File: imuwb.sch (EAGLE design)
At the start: 13 parts

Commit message: new version
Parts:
- added C4: 100nf, ipc-7351-capacitor:CAPACITOR_0402
- added U$1: MIC53533.3V, bell-card:MIC53533.3V
- added U$2: BATPADS, custom:BATPADS
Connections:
- net CSE renamed CS_ENV
- removed net CS: DWM.CS, MCP2210.GP6
- removed net CSB: BMF.PA00, MCP2210.GP2
- removed net IRQ: BMF.PA22, DWM.GPIO8/IRQ
- removed net RSTN: DWM.RSTN
- removed net RST_MCP: BMF.PA20, MCP2210.RST, R1.1
- removed net SUSP: BMF.PA01, MCP2210.GP1
- new net CS_ACC: BMF.PA18/CSB_ACC, MCP2210.GP0
- new net CS_DWM: DWM.CS, MCP2210.GP7
- new net CS_GYR: BMF.PA27/CSB_GYRO, MCP2210.GP1
- new net IRQ_DW: BMF.PA22, DWM.GPIO8/IRQ, MCP2210.GP6
- new net N$4: C4.2, U$1.BYP
- new net N$5: MCP2210.RST, R1.1
- new net VBAT: AAT3681.BAT, C3.1, U$1.EN, U$1.VIN, U$2.-
- net +3V3: now also MCP2210.VUSB, U$1.VOUT; no longer AAT3681.BAT, AAT3681.EN, BMF.PB02, C3.2
- net GND: now also C3.2, C4.1, U$1.GND, U$1.GND1, U$2.+; no longer C3.1
- net RESET: now also DWM.RSTN, MCP2210.GP2
- net VBUS: now also AAT3681.EN; no longer MCP2210.VUSB
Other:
- note added: "ERRATA:"
- note added: "battery connector"
- note added: "voltage regulator"
- note removed: "ERRATA: * GP2 is USB SUSPEND, exchange GP1/GP2 * GP6 is IRQIN, wire to IRQ * wire RST pins for initialization? * move pins below mcp2210"
- note removed: "bat charge estimation"
- note removed: "necc to regulate voltage level below 4.2v all time (i.e. when USB only, when BAT only, when USB+BAT)"
- moved on the sheet: C3

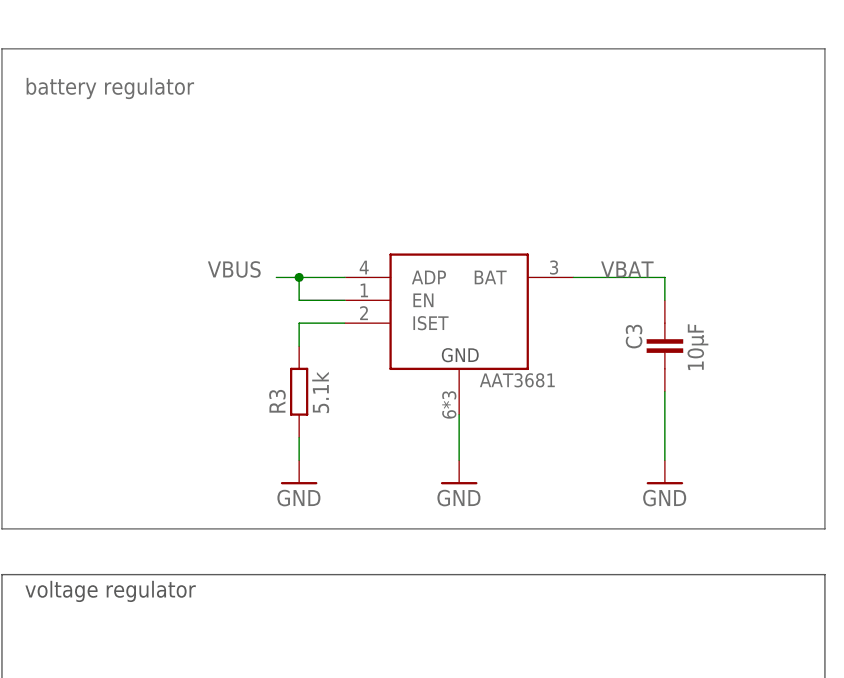
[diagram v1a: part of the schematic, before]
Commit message: updates to the BOM
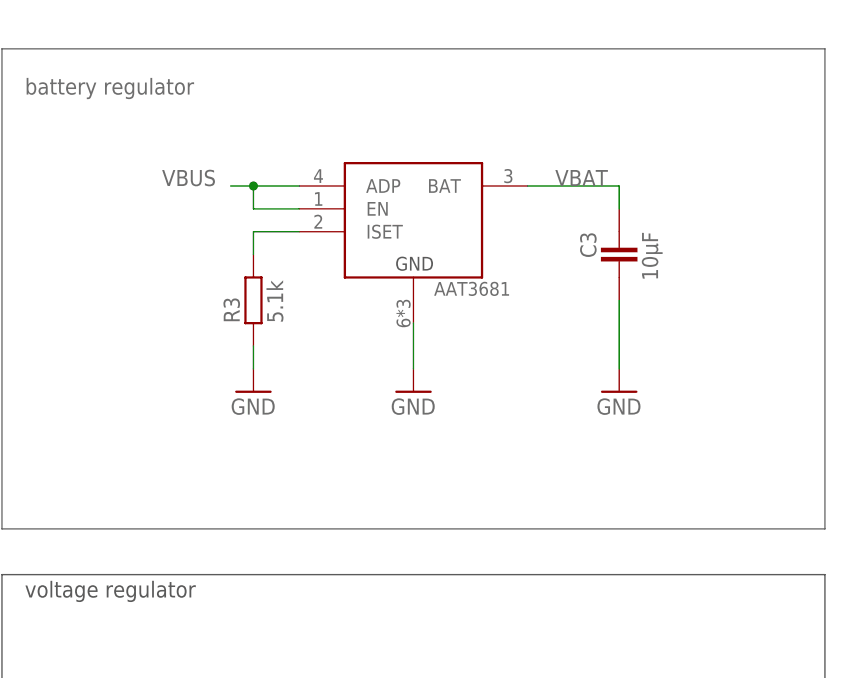
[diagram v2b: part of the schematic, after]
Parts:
- OSC: PARTNO (none) -> PRQC12.00CR1010V00L
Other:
- moved on the sheet: AAT3681, C3, R3
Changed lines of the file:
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@@
 <part name="+3V3" library="supply1" deviceset="+3V3" device=""/>
 <part name="GND6" library="supply1" deviceset="GND" device=""/>
-<part name="OSC" library="custom" deviceset="CSTCE" device=""/>
+<part name="OSC" library="custom" deviceset="CSTCE" device="">
+<attribute name="PARTNO" value="PRQC12.00CR1010V00L"/>
+</part>
 <part name="C1" library="ipc-7351-capacitor" deviceset="CAPACITOR_" device="0402" value="100nf"/>
 <part name="C2" library="ipc-7351-capacitor" deviceset="CAPACITOR_" device="0402" value="100nf"/>
@@
 <instance part="R2" gate="G$1" x="195.58" y="129.54" rot="R90"/>
 <instance part="GND7" gate="1" x="195.58" y="139.7" rot="R180"/>
-<instance part="AAT3681" gate="G$1" x="264.16" y="116.84">
-<attribute name="PARTNO" x="264.16" y="116.84" size="1.778" layer="96" display="off"/>
+<instance part="AAT3681" gate="G$1" x="259.08" y="127">
+<attribute name="PARTNO" x="259.08" y="127" size="1.778" layer="96" display="off"/>
 </instance>
-<instance part="GND8" gate="1" x="264.16" y="96.52"/>
-<instance part="C3" gate="G$1" x="287.02" y="111.76" rot="MR270"/>
-<instance part="GND9" gate="1" x="287.02" y="96.52"/>
-<instance part="R3" gate="G$1" x="246.38" y="106.68" rot="R90"/>
-<instance part="GND10" gate="1" x="246.38" y="96.52"/>
+<instance part="GND8" gate="1" x="259.08" y="106.68"/>
+<instance part="C3" gate="G$1" x="281.94" y="121.92" rot="MR270"/>
+<instance part="GND9" gate="1" x="281.94" y="106.68"/>
+<instance part="R3" gate="G$1" x="241.3" y="116.84" rot="R90"/>
+<instance part="GND10" gate="1" x="241.3" y="106.68"/>
 <instance part="+3V10" gate="G$1" x="294.64" y="48.26" rot="R270"/>
 <instance part="GND11" gate="1" x="294.64" y="63.5" rot="R90"/>
@@
 <pinref part="GND8" gate="1" pin="GND"/>
 <pinref part="AAT3681" gate="G$1" pin="GND"/>
-<wire x1="264.16" y1="99.06" x2="264.16" y2="104.14" width="0.1524" layer="91"/>
+<wire x1="259.08" y1="109.22" x2="259.08" y2="114.3" width="0.1524" layer="91"/>
 </segment>
 <segment>
 <pinref part="GND10" gate="1" pin="GND"/>
 <pinref part="R3" gate="G$1" pin="1"/>
-<wire x1="246.38" y1="99.06" x2="246.38" y2="101.6" width="0.1524" layer="91"/>
+<wire x1="241.3" y1="109.22" x2="241.3" y2="111.76" width="0.1524" layer="91"/>
 </segment>
 <segment>
@@
 <pinref part="GND9" gate="1" pin="GND"/>
 <pinref part="C3" gate="G$1" pin="2"/>
-<wire x1="287.02" y1="99.06" x2="287.02" y2="106.68" width="0.1524" layer="91"/>
+<wire x1="281.94" y1="109.22" x2="281.94" y2="116.84" width="0.1524" layer="91"/>
 </segment>
 </net>
@@
 <segment>
 <pinref part="AAT3681" gate="G$1" pin="ADP"/>
-<wire x1="251.46" y1="119.38" x2="246.38" y2="119.38" width="0.1524" layer="91"/>
-<label x="236.22" y="119.38" size="1.778" layer="95"/>
+<wire x1="246.38" y1="129.54" x2="241.3" y2="129.54" width="0.1524" layer="91"/>
+<label x="231.14" y="129.54" size="1.778" layer="95"/>
 <pinref part="AAT3681" gate="G$1" pin="EN"/>
-<wire x1="246.38" y1="119.38" x2="243.84" y2="119.38" width="0.1524" layer="91"/>
-<wire x1="251.46" y1="116.84" x2="246.38" y2="116.84" width="0.1524" layer="91"/>
-<wire x1="246.38" y1="116.84" x2="246.38" y2="119.38" width="0.1524" layer="91"/>
-<junction x="246.38" y="119.38"/>
+<wire x1="241.3" y1="129.54" x2="238.76" y2="129.54" width="0.1524" layer="91"/>
+<wire x1="246.38" y1="127" x2="241.3" y2="127" width="0.1524" layer="91"/>
+<wire x1="241.3" y1="127" x2="241.3" y2="129.54" width="0.1524" layer="91"/>
+<junction x="241.3" y="129.54"/>
 </segment>
 </net>
@@
 <pinref part="AAT3681" gate="G$1" pin="ISET"/>
 <pinref part="R3" gate="G$1" pin="2"/>
-<wire x1="251.46" y1="114.3" x2="246.38" y2="114.3" width="0.1524" layer="91"/>
-<wire x1="246.38" y1="114.3" x2="246.38" y2="111.76" width="0.1524" layer="91"/>
+<wire x1="246.38" y1="124.46" x2="241.3" y2="124.46" width="0.1524" layer="91"/>
+<wire x1="241.3" y1="124.46" x2="241.3" y2="121.92" width="0.1524" layer="91"/>
 </segment>
 </net>
@@
 <segment>
 <pinref part="AAT3681" gate="G$1" pin="BAT"/>
-<label x="279.908" y="119.38" size="1.778" layer="95"/>
+<label x="274.828" y="129.54" size="1.778" layer="95"/>
 <pinref part="C3" gate="G$1" pin="1"/>
-<wire x1="276.86" y1="119.38" x2="287.02" y2="119.38" width="0.1524" layer="91"/>
-<wire x1="287.02" y1="119.38" x2="287.02" y2="116.84" width="0.1524" layer="91"/>
-</segment>
-</net>
+<wire x1="271.78" y1="129.54" x2="281.94" y2="129.54" width="0.1524" layer="91"/>
+<wire x1="281.94" y1="129.54" x2="281.94" y2="127" width="0.1524" layer="91"/>
+</segment>
+</net>
